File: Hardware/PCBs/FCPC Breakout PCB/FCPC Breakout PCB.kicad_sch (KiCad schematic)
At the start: 12 parts, among them J1 CAN, J10 RS485, J2 RS485, J3 UART, J4 5V, J5 12V, J6 UART, J7 CAN, J8 5V, J9 12V

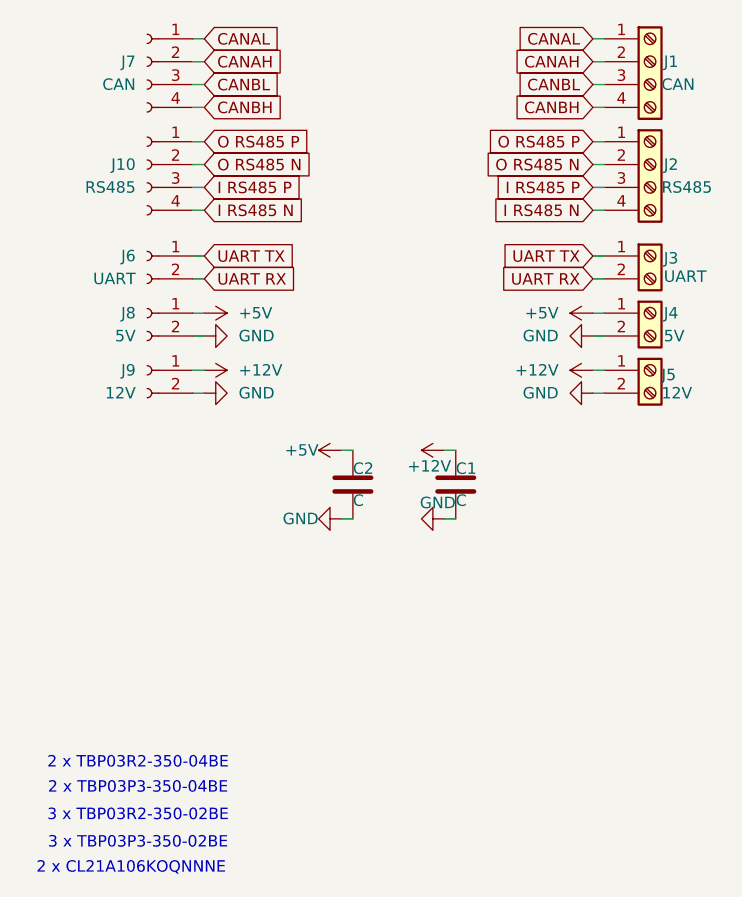
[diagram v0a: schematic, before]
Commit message: PCB Update
UART Voltage Divider 5V -> 3.3V
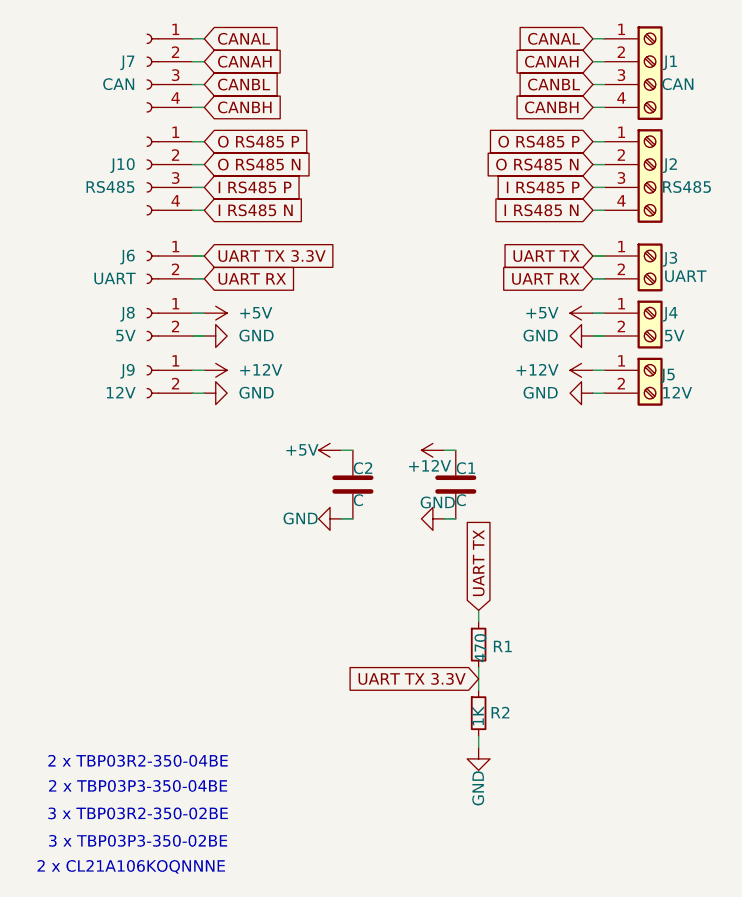
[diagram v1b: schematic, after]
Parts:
- added R1: 470, Resistor_SMD:R_0805_2012Metric_Pad1.20x1.40mm_HandSolder, symbol Device:R_Small
- added R2: 1K, Resistor_SMD:R_0805_2012Metric_Pad1.20x1.40mm_HandSolder, symbol Device:R_Small
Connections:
- net GND: now also R2.2
- net UART TX: now also R1.1; no longer J6.1 (Pin_1)
- new net UART TX 3.3V: J6.1 (Pin_1), R1.2, R2.1
